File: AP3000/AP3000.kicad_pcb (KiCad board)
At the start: 4 copper layers, 186 x 226 mm, 183 parts, among them IC2 TPS23751PWPR, J1 Conn_01x03, J11 Barrel_Jack, J12 Bus_PCI_Express_Mini, J2 Conn_02x07_Odd_Even, J3 Conn_01x03, J4 Conn_01x22_Female, J5 Conn_01x22_Female, J6 THD-02-R, J7 YJ-USB-AF_SMT-01, J8 THD-20-R, J9 0826-1X1T-GH-F, Q1 BSC520N15NS3 G, Q2 MMBT2907ALT1G, Q3 MMBT3906LT1G, U1 TPD4EUSB30, U10 SIR422DP-T1-GE3, U12 TCMT1107, U13 TLV431ACDBZR, U14 74LVC1G07SE-7, U16 TPS54A24RTWR, U17 TPS628640AYCGR, U2 TPD4EUSB30, U4 TPD4EUSB30, U5 74LVC1G07SE-7, U7 AP22653W6, U8 PCF85063AT/AAZ, U9 74LVC1G07SE-7, Y2 X32K768S301

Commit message: Route all the high speed lines and most gpio
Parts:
- moved U4 0.19 mm to (96.5, 135.4)
- moved C5 0.12 mm to (176.6, 163.4)
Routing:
- net /CM4_GPIO ( Ethernet, GPIO, SDCARD)/GPIO26: track 0.00 -> 71.1 mm
- net /CM4_GPIO ( Ethernet, GPIO, SDCARD)/GPIO13: track 0.00 -> 68.9 mm
- net /CM4_GPIO ( Ethernet, GPIO, SDCARD)/GPIO19: track 0.00 -> 67.2 mm
- net /PCIE_TX_P: track 0.00 -> 66.3 mm, vias 0 -> 2
- net /PCIE_TX_N: track 0.00 -> 65.9 mm, vias 0 -> 2
- net /PCIE_RX_P: track 0.00 -> 63.6 mm, vias 0 -> 2
- net /PCIE_RX_N: track 0.00 -> 63.3 mm, vias 0 -> 2
- net /CM4_GPIO ( Ethernet, GPIO, SDCARD)/GPIO21: track 0.00 -> 58.8 mm, vias 0 -> 2
- net /CM4_HighSpeed/CAM1_D0_N: track 0.00 -> 57.3 mm
- net /CM4_HighSpeed/CAM1_D0_P: track 0.00 -> 56.8 mm
- net /CM4_GPIO ( Ethernet, GPIO, SDCARD)/GPIO20: track 0.00 -> 56.3 mm, vias 0 -> 2
- net /CM4_HighSpeed/CAM1_D1_N: track 0.00 -> 55.7 mm
- net /PCIE_CLK_P: track 0.00 -> 55.4 mm
- net /CM4_HighSpeed/CAM1_D1_P: track 0.00 -> 55.4 mm
- net /PCIE_CLK_N: track 0.00 -> 55.0 mm
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
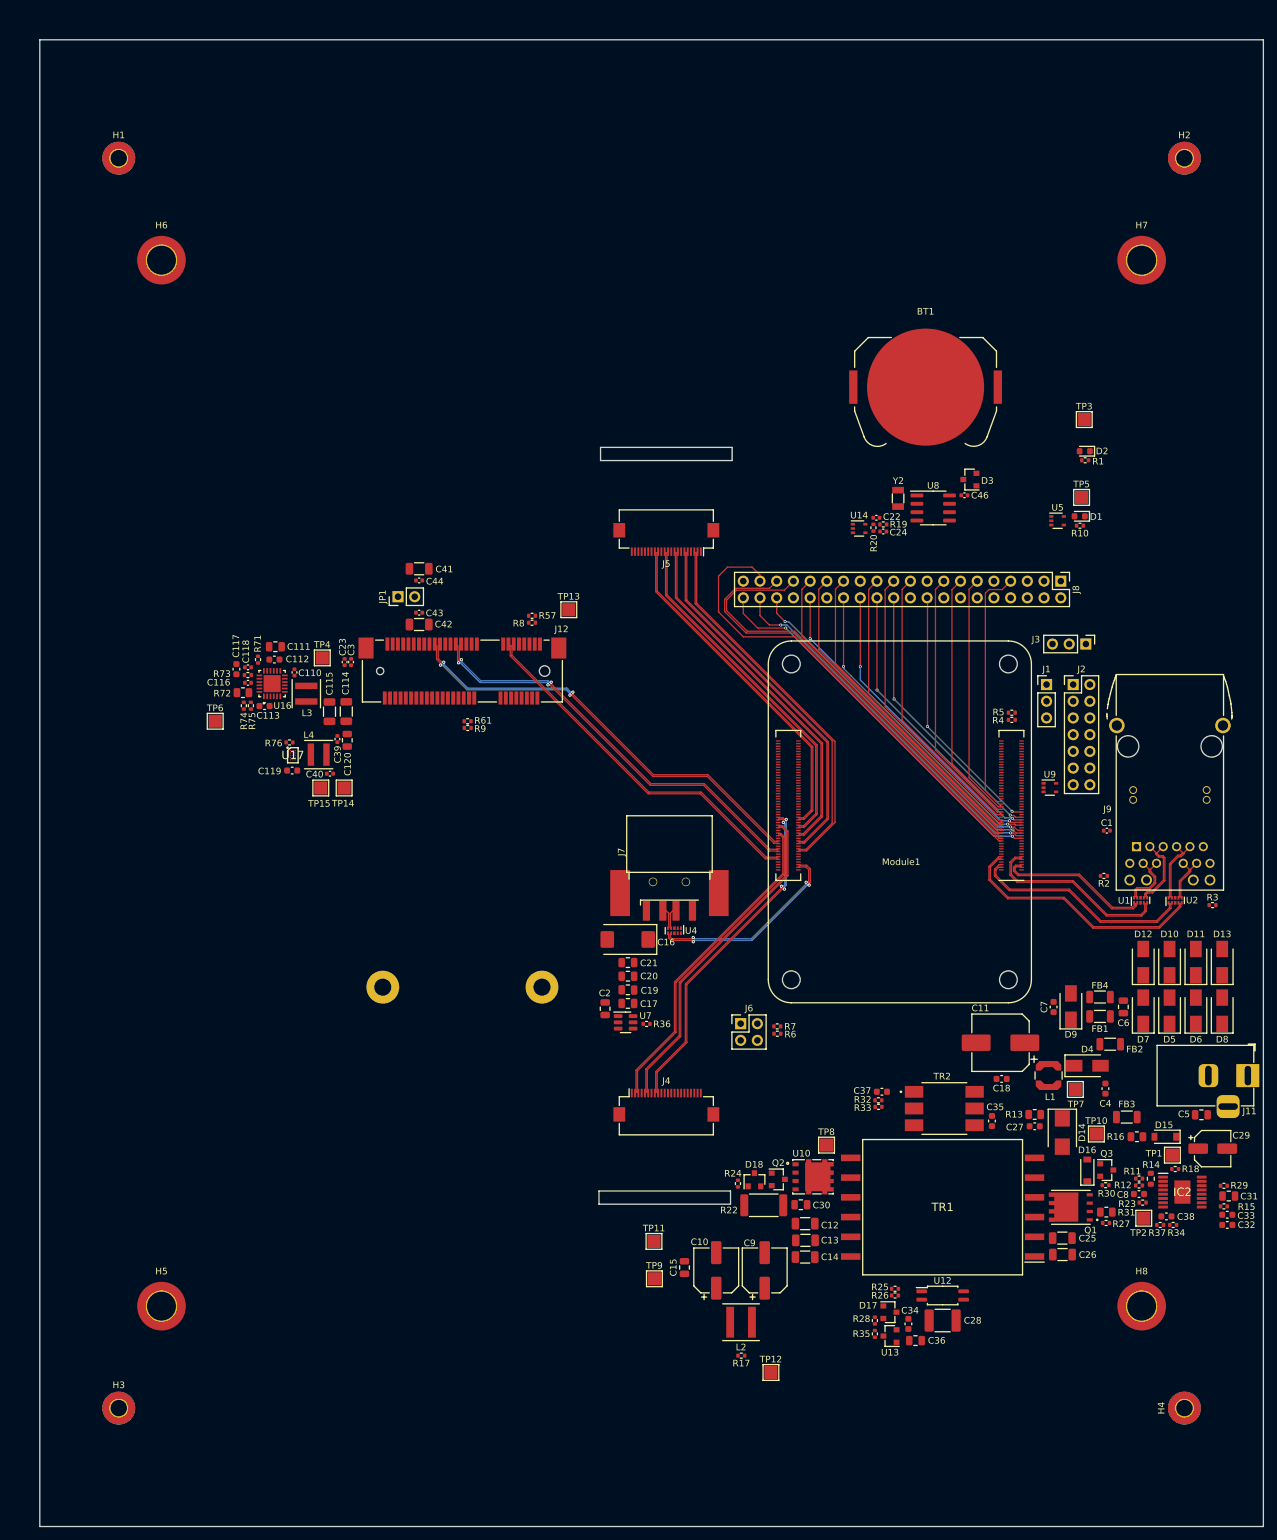
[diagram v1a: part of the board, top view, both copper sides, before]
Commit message: Forgot to add PCB cutout resulting in some components being moved
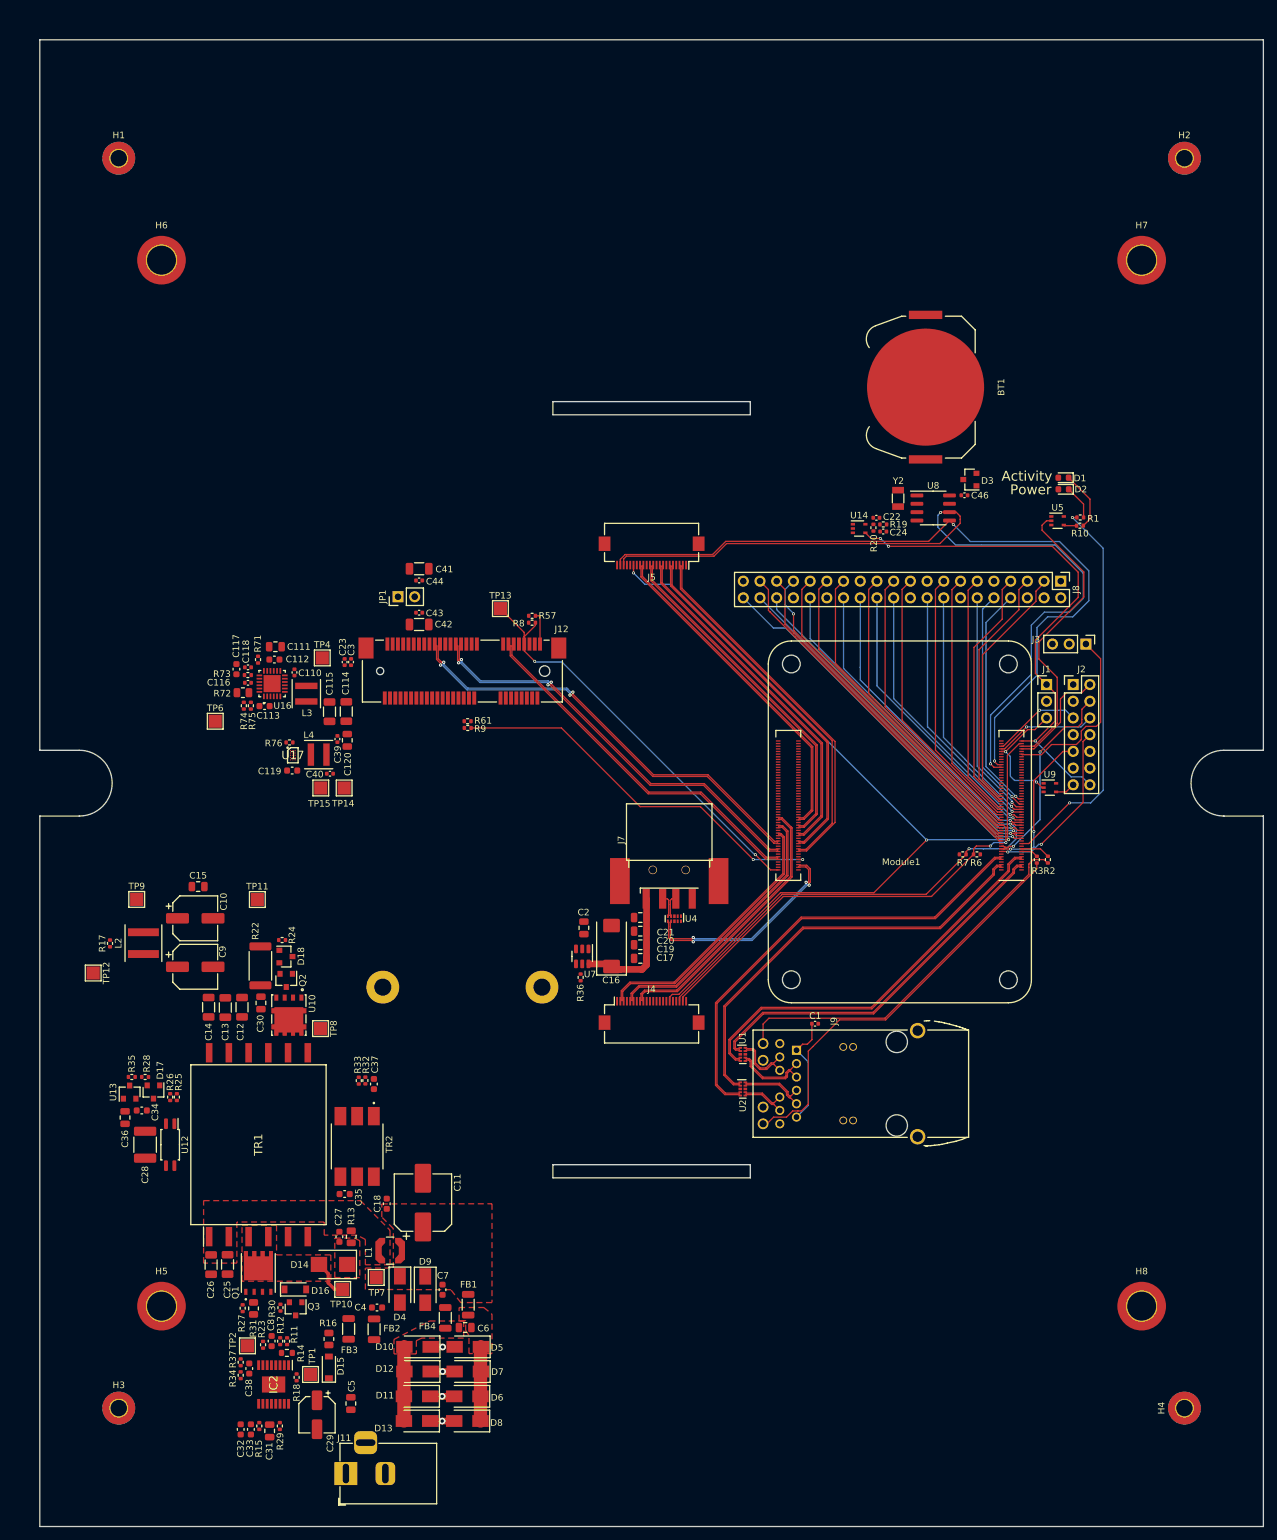
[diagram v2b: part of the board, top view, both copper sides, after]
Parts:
- removed J6: THD-02-R, Connector_PinHeader_2.54mm:PinHeader_2x02_P2.54mm_Vertical
- removed R4: DNS 0, Resistor_SMD:R_0402_1005Metric
- removed R5: 0R, Resistor_SMD:R_0402_1005Metric
- removed TP3, TP5: TestPoint, TestPoint:TestPoint_Pad_2.0x2.0mm
- moved C32 153.2 mm to (30.5, 211.2), turned to -90 degrees
- moved C33 152.0 mm to (32.1, 211.2), turned to -90 degrees
- moved R15 150.4 mm to (33.4, 210.7), turned to 90 degrees
- moved C31 150.1 mm to (34.9, 211.5), turned to -90 degrees
- moved J11 149.9 mm to (46.5, 217.9), turned to 180 degrees
- moved R29 148.1 mm to (36.5, 210.7), turned to -90 degrees
- moved R34 143.6 mm to (30.5, 203.0), turned to 90 degrees
- moved C29 142.0 mm to (42.1, 209.0), turned to -90 degrees
- moved C38 141.3 mm to (31.8, 202.0), turned to 90 degrees
- moved R37 141.3 mm to (30.5, 201.0), turned to -90 degrees
- moved IC2 141.2 mm to (35.5, 204.4), turned to -90 degrees
- moved D13 140.9 mm to (57.4, 210.0), turned to 180 degrees
- moved TP2 137.6 mm to (31.6, 198.5), turned to -90 degrees
- moved R18 137.3 mm to (39.0, 203.3), turned to -90 degrees
- moved C5 136.5 mm to (47.3, 207.3), turned to 90 degrees
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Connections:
- J4 pad 20: /CM4_HighSpeed/SCL1 -> /ID_SC
- J4 pad 21: /CM4_HighSpeed/SDA1 -> /ID_SD
- Module1 pad 78: /GPIO_VREF -> /+3.3v
- R6 pad 1: /GPIO_VREF -> /+3.3v
- R6 pad 2: /CM4_HighSpeed/SDA1 -> /ID_SD
- R7 pad 1: /GPIO_VREF -> /+3.3v
- R7 pad 2: /CM4_HighSpeed/SCL1 -> /ID_SC
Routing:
- net /CAM_GPIO: track 0.00 -> 140.4 mm, vias 0 -> 3
- net /SCL0: track 0.00 -> 125.0 mm, vias 0 -> 2
- net /SDA0: track 0.00 -> 116.1 mm, vias 0 -> 2
- net /TR2_TAP: track 0.00 -> 94.2 mm, vias 0 -> 1
- net /TR3_TAP: track 0.00 -> 91.1 mm, vias 0 -> 1
- net /TR0_TAP: track 0.00 -> 87.3 mm, vias 0 -> 1
- net /TR1_TAP: track 0.00 -> 86.3 mm, vias 0 -> 1
- net /GLOBAL_EN: track 0.00 -> 78.9 mm, vias 0 -> 3
- net /ID_SC: track 47.7 -> 112.5 mm
- net /PCIE_CLK_nREQ: track 0.00 -> 64.3 mm, vias 0 -> 2
- net Net-(J9-Pad20): track 0.00 -> 63.3 mm
- net /ID_SD: track 48.4 -> 111.6 mm, vias 0 -> 2
- net Net-(Module1-Pad21): track 0.00 -> 59.9 mm, vias 0 -> 2
- net /PCIE_nRST: track 0.00 -> 59.4 mm, vias 0 -> 2
- net Net-(J9-Pad17): track 0.00 -> 57.7 mm
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- added copper zone on F.Cu, net /PoE/VDD
- added copper zone on F.Cu, net Net-(C25-Pad1)
- added copper zone on F.Cu, net Net-(C27-Pad2)
- added copper zone on F.Cu, net Net-(C6-Pad1)
- added copper zone on F.Cu, net Net-(C6-Pad2)
- added copper zone on F.Cu, net Net-(D14-Pad2)
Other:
- outline, holes or cut-outs redrawn
- board text added: "Activity"
- board text added: "Power"

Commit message: Route more
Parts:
- J4: value Conn_01x22_Female -> Camera 0; footprint Connector_FFC-FPC:Hirose_FH12-22S-0.5SH_1x22-1MP_P0.50mm_Horizontal -> AP3000:EDAC 690-019-298-412
- J5: value Conn_01x22_Female -> Camera 1; footprint Connector_FFC-FPC:Hirose_FH12-22S-0.5SH_1x22-1MP_P0.50mm_Horizontal -> AP3000:EDAC 690-019-298-412
- moved R29 19.1 mm to (41.2, 192.3), turned to 90 degrees
- moved TP7 16.3 mm to (65.5, 180.3)
- moved BT1 12.4 mm to (146.8, 50.4)
- moved C5 6.53 mm to (48.3, 200.8), turned to 180 degrees
- moved C29 5.47 mm to (39.3, 213.7)
- moved C32 3.67 mm to (31.1, 207.6), turned to 0 degrees
- moved C4 2.98 mm to (48.3, 192.8)
- moved D4 2.36 mm to (53.1, 188.2), turned to 180 degrees
- moved TP12 1.99 mm to (10.0, 141.3)
- moved J11 1.55 mm to (48.0, 217.6)
- moved D15 1.35 mm to (45.2, 202.2)
- moved FB2 1.18 mm to (49.6, 196.0)
- moved R16 1.11 mm to (44.6, 196.6)
- moved C15 0.96 mm to (23.1, 128.8)
- moved R17 0.95 mm to (9.99, 136.7)
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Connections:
- J4 pad 1: GND -> Net-(J4-Pad1)
- J4 pad 10: GND -> /CM4_HighSpeed/CAM0_C_P
- J4 pad 11: Net-(J4-Pad11) -> GND
- J4 pad 12: Net-(J4-Pad12) -> /CM4_HighSpeed/CAM0_C_N
- J4 pad 13: GND -> /CAM_GPIO
- J4 pad 15: Net-(J4-Pad15) -> /ID_SC
- J4 pad 16: GND -> /ID_SD
- J4 pad 17: /CAM_GPIO -> GND
- J4 pad 18: Net-(J4-Pad18) -> /+3.3v
- J4 pad 19: GND -> Net-(J4-Pad19)
- J4 pad 2: /CM4_HighSpeed/CAM0_D0_N -> GND
- J4 pad 3: /CM4_HighSpeed/CAM0_D0_P -> Net-(J4-Pad3)
- J4 pad 4: GND -> /CM4_HighSpeed/CAM0_D1_P
- J4 pad 5: /CM4_HighSpeed/CAM0_D1_N -> GND
- J4 pad 6: /CM4_HighSpeed/CAM0_D1_P -> /CM4_HighSpeed/CAM0_D1_N
- J4 pad 7: GND -> /CM4_HighSpeed/CAM0_D0_P
- J4 pad 8: /CM4_HighSpeed/CAM0_C_N -> GND
- J4 pad 9: /CM4_HighSpeed/CAM0_C_P -> /CM4_HighSpeed/CAM0_D0_N
- J5 pad 1: GND -> /CM4_HighSpeed/CAM1_D2_P
- J5 pad 10: GND -> /CM4_HighSpeed/CAM1_C_P
- J5 pad 11: /CM4_HighSpeed/CAM1_D2_N -> GND
- J5 pad 12: /CM4_HighSpeed/CAM1_D2_P -> /CM4_HighSpeed/CAM1_C_N
- J5 pad 13: GND -> /CAM_GPIO
- J5 pad 14: /CM4_HighSpeed/CAM1_D3_N -> /CM4_HighSpeed/CAM1_D3_P
- J5 pad 15: /CM4_HighSpeed/CAM1_D3_P -> /SCL0
- J5 pad 16: GND -> /SDA0
- J5 pad 17: /CAM_GPIO -> GND
- J5 pad 18: Net-(J5-Pad18) -> /+3.3v
- J5 pad 19: GND -> /CM4_HighSpeed/CAM1_D3_N
- J5 pad 2: /CM4_HighSpeed/CAM1_D0_N -> GND
- J5 pad 3: /CM4_HighSpeed/CAM1_D0_P -> /CM4_HighSpeed/CAM1_D2_N
- J5 pad 4: GND -> /CM4_HighSpeed/CAM1_D1_P
- J5 pad 5: /CM4_HighSpeed/CAM1_D1_N -> GND
- J5 pad 6: /CM4_HighSpeed/CAM1_D1_P -> /CM4_HighSpeed/CAM1_D1_N
- J5 pad 7: GND -> /CM4_HighSpeed/CAM1_D0_P
- J5 pad 8: /CM4_HighSpeed/CAM1_C_N -> GND
- J5 pad 9: /CM4_HighSpeed/CAM1_C_P -> /CM4_HighSpeed/CAM1_D0_N
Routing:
- net /PoE/VC: track 0.00 -> 58.1 mm, vias 0 -> 6
- net Net-(C35-Pad1): track 0.00 -> 51.9 mm, vias 0 -> 3
- net /+1.5v: track 0.00 -> 49.0 mm, vias 0 -> 6
- net Net-(BT1-Pad1): track 0.00 -> 48.8 mm
- net /PoE/VDD: track 0.00 -> 47.8 mm, vias 0 -> 3
- net Net-(C38-Pad2): track 0.00 -> 37.1 mm, vias 0 -> 2
- net Net-(C5-Pad2): track 0.00 -> 36.6 mm
- net Net-(D17-Pad2): track 0.00 -> 31.4 mm
- net Net-(D18-Pad3): track 0.00 -> 26.4 mm
- net Net-(C33-Pad1): track 0.00 -> 24.6 mm
- net Net-(C5-Pad1): track 0.00 -> 20.7 mm
- net Net-(R16-Pad2): track 0.00 -> 19.0 mm, vias 0 -> 6
- net Net-(C34-Pad1): track 0.00 -> 17.8 mm
- net Net-(C4-Pad1): track 0.00 -> 14.3 mm
- net /PoE/VB: track 0.00 -> 13.5 mm
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- added copper zone on F.Cu, net /+1.5v
- added copper zone on F.Cu, net /+3.3v
- added copper zone on F.Cu, net /+5v
- added copper zone on In2.Cu, net /+5v
- added copper zone on B.Cu, net /PoE/VSS
- added copper zone on F.Cu, net /PoE/VSS
- added copper zone on In1.Cu, net /PoE/VSS
- added copper zone on In2.Cu, net /PoE/VSS
- added copper zone on F.Cu, net Net-(C110-Pad2)
- added copper zone on F.Cu, net Net-(C12-Pad1)
- added copper zone on F.Cu, net Net-(C30-Pad1)
- added copper zone on F.Cu, net Net-(C4-Pad1)
- added copper zone on F.Cu, net Net-(J12-Pad45)
- added copper zone on F.Cu, net Net-(L4-Pad1)
- added copper zone on F.Cu, net Net-(Q1-Pad1)
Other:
- outline, holes or cut-outs redrawn

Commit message: Almost done routing!
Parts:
- added J10: Camera 1 Power, Connectors:SCREWTERMINAL-5MM-2, F.Cu at (75.9, 76.4)
- added J6: Camera 1, Connector_RJ:RJ45_Amphenol_54602-x08_Horizontal, F.Cu at (97.6, 82.5)
- J4: footprint AP3000:EDAC 690-019-298-412 -> Connector_RJ:RJ45_Amphenol_54602-x08_Horizontal
- J5: value Camera 1 -> Camera 0 Power; footprint AP3000:EDAC 690-019-298-412 -> Connectors:SCREWTERMINAL-5MM-2
- moved J5 77.9 mm to (80.1, 154.9)
- moved TP6 22.4 mm to (43.8, 89.3)
- moved J4 4.03 mm to (89.0, 148.5)
- moved R61 1.13 mm to (65.0, 102.5)
- moved R9 1.10 mm to (65.0, 103.5)
- moved TP4 1.07 mm to (43.9, 93.6)
- moved FB1 0.57 mm to (65.6, 192.0)
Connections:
- H1 pad 1: GND -> Net-(H1-Pad1)
- H2 pad 1: GND -> Net-(H2-Pad1)
- H3 pad 1: GND -> Net-(H3-Pad1)
- H4 pad 1: GND -> Net-(H4-Pad1)
- H5 pad 1: GND -> Net-(H5-Pad1)
- H6 pad 1: GND -> Net-(H6-Pad1)
- H7 pad 1: GND -> Net-(H7-Pad1)
- H8 pad 1: GND -> Net-(H8-Pad1)
- J4 pad 1: Net-(J4-Pad1) -> /CM4_HighSpeed/CAM0_D0_P
- J4 pad 2: GND -> /CM4_HighSpeed/CAM0_D0_N
- J4 pad 3: Net-(J4-Pad3) -> /CM4_HighSpeed/CAM0_D1_P
- J4 pad 4: /CM4_HighSpeed/CAM0_D1_P -> /CM4_HighSpeed/CAM0_D1_N
- J4 pad 5: GND -> /CM4_HighSpeed/CAM0_C_P
- J4 pad 6: /CM4_HighSpeed/CAM0_D1_N -> /CM4_HighSpeed/CAM0_C_N
- J4 pad 7: /CM4_HighSpeed/CAM0_D0_P -> /ID_SC
- J4 pad 8: GND -> /ID_SD
- J5 pad 1: /CM4_HighSpeed/CAM1_D2_P -> /+3.3v
- Module1 pad 133: /CM4_HighSpeed/CAM1_D2_N -> Net-(Module1-Pad133)
- Module1 pad 135: /CM4_HighSpeed/CAM1_D2_P -> Net-(Module1-Pad135)
- Module1 pad 139: /CM4_HighSpeed/CAM1_D3_N -> Net-(Module1-Pad139)
- Module1 pad 141: /CM4_HighSpeed/CAM1_D3_P -> Net-(Module1-Pad141)
- Module1 pad 97: /CAM_GPIO -> Net-(Module1-Pad97)
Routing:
- net /CAM_GPIO: track 146.4 -> 0.00 mm, vias 5 -> 0
- net /CM4_HighSpeed/CAM1_D2_N: track 56.6 -> 0.00 mm
- net /CM4_HighSpeed/CAM1_D2_P: track 56.2 -> 0.00 mm
- net /CM4_HighSpeed/CAM1_D3_N: track 51.2 -> 0.00 mm, vias 2 -> 0
- net /CM4_HighSpeed/CAM1_D3_P: track 50.8 -> 0.00 mm, vias 2 -> 0
- net /+3.3v: track 13.1 -> 55.6 mm, vias 0 -> 21
- net /CM4_GPIO ( Ethernet, GPIO, SDCARD)/BT_nDis: track 0.00 -> 21.0 mm, vias 0 -> 2
- net /+5v: track 11.6 -> 25.9 mm, vias 33 -> 53
- net /ID_SD: track 123.8 -> 112.2 mm, vias 3 -> 2
- net /ID_SC: track 121.0 -> 113.7 mm, vias 3 -> 2
- net /CM4_HighSpeed/CAM0_D0_P: track 35.6 -> 41.1 mm
- net /PoE/T2P: track 0.00 -> 5.45 mm
- net /CM4_HighSpeed/CAM0_D0_N: track 35.2 -> 40.2 mm
- net /SCL0: track 114.8 -> 110.2 mm, vias 3 -> 2
- net /SDA0: track 110.5 -> 115.0 mm, vias 3 -> 2
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- added copper zone on In2.Cu, net /+3.3v
- added copper zone on B.Cu, net /+5v
- added copper zone on B.Cu, net GND
- added copper zone on F.Cu, net GND
- added copper zone on In1.Cu, net GND
- added copper zone on In2.Cu, net GND
- added copper zone on B.Cu, net GNDPWR
- added copper zone on F.Cu, net GNDPWR
- removed copper zone on In2.Cu, net /+5v
- removed copper zone on B.Cu, net /PoE/VSS

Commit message: Finished routing board.
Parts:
- added C45: .1uF, Capacitor_SMD:C_0402_1005Metric, F.Cu at (135.5, 74.5)
- added H10: Mounting Hole, MountingHole:MountingHole_2.5mm_Pad_TopBottom, F.Cu at (93.0, 5.00)
- added H11: Mounting Hole, MountingHole:MountingHole_2.5mm_Pad_TopBottom, F.Cu at (16.0, 113.0)
- added H12: Mounting Hole, MountingHole:MountingHole_2.5mm_Pad_TopBottom, F.Cu at (170.0, 113.0)
- added H9: Mounting Hole, MountingHole:MountingHole_2.5mm_Pad_TopBottom, F.Cu at (93.0, 221.0)
- added U3: ATECC608A-MAHDA, Package_DFN_QFN:DFN-8-1EP_3x2mm_P0.5mm_EP1.3x1.5mm, F.Cu at (134.3, 76.4)
- moved TP13 58.2 mm to (56.0, 143.0), turned to 180 degrees
- moved R57 57.7 mm to (51.3, 140.2), turned to -90 degrees
- moved R8 56.3 mm to (52.4, 140.2), turned to -90 degrees
- moved JP1 51.1 mm to (83.8, 126.3), turned to 180 degrees
- moved C2 48.5 mm to (127.1, 154.6), turned to -90 degrees
- moved C44 47.3 mm to (81.3, 123.0), turned to 90 degrees
- moved C41 46.9 mm to (79.6, 122.2), turned to 90 degrees
- moved U7 46.2 mm to (127.3, 150.3), turned to 90 degrees
- moved R36 46.1 mm to (128.1, 147.6), turned to 0 degrees
- moved C43 46.1 mm to (86.1, 123.1), turned to 90 degrees
- moved C42 44.8 mm to (87.9, 122.3), turned to 90 degrees
- moved J7 44.2 mm to (114.2, 164.9), turned to -90 degrees
- moved C16 38.6 mm to (122.9, 151.8), turned to -90 degrees
- moved J12 37.6 mm to (61.8, 133.5), turned to 0 degrees
- moved C21 35.4 mm to (118.5, 156.2), turned to 0 degrees
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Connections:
- J12 pad 23: /PCIE_RX_N -> /PCIE_RX_P
- J12 pad 25: /PCIE_RX_P -> /PCIE_RX_N
- J12 pad 31: /PCIE_TX_N -> /PCIE_TX_P
- J12 pad 33: /PCIE_TX_P -> /PCIE_TX_N
- J9 pad 21: GND -> GNDPWR
- J9 pad 22: GND -> GNDPWR
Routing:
- net /CM4_GPIO ( Ethernet, GPIO, SDCARD)/E0_TRD0_P: track 75.9 -> 44.2 mm
- net /CM4_GPIO ( Ethernet, GPIO, SDCARD)/E0_TRD0_N: track 75.1 -> 43.8 mm
- net /CM4_GPIO ( Ethernet, GPIO, SDCARD)/E0_TRD1_N: track 74.5 -> 45.2 mm
- net /CM4_GPIO ( Ethernet, GPIO, SDCARD)/E0_TRD1_P: track 73.7 -> 44.8 mm
- net /CM4_GPIO ( Ethernet, GPIO, SDCARD)/E0_TRD2_P: track 71.6 -> 47.7 mm
- net /CM4_GPIO ( Ethernet, GPIO, SDCARD)/E0_TRD2_N: track 70.8 -> 47.3 mm
- net /CM4_GPIO ( Ethernet, GPIO, SDCARD)/E0_TRD3_N: track 65.7 -> 43.3 mm
- net /CM4_GPIO ( Ethernet, GPIO, SDCARD)/E0_TRD3_P: track 64.9 -> 43.0 mm
- net Net-(J12-Pad45): track 0.00 -> 20.0 mm
- net Net-(J9-Pad17): track 57.7 -> 39.4 mm
- net /PCIE_CLK_N: track 55.0 -> 72.7 mm
- net /PCIE_CLK_P: track 55.4 -> 72.7 mm
- net /TR3_TAP: track 101.2 -> 84.4 mm
- net Net-(J9-Pad20): track 63.3 -> 49.5 mm, vias 0 -> 1
- net /TR1_TAP: track 95.3 -> 82.3 mm
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- added copper zone on In1.Cu, net /+5v
- added copper zone on In1.Cu, net GNDPWR
- added copper zone on In2.Cu, net GNDPWR
- removed copper zone on B.Cu, net /+5v
- removed copper zone on F.Cu, net Net-(J12-Pad45)
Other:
- outline, holes or cut-outs redrawn
- board text added: "+"
- board text added: "-"
- board text added: "AP3000 V3 Copyright 2020 ISis ImageStream Internet Solutions, Inc."
- board text added: "Camera 0"
- board text added: "Camera 1"
- board text added: "DC In (21.6v-57v)"
- board text added: "Designed by Scott Yoder"
- board text added: "Ethernet0"
- board text added: "USB"
